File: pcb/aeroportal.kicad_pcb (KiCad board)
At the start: 2 copper layers, 80 x 70 mm, 4 parts, among them J1 MAX98357A Breakout Board, U1 WEMOS_C3_Mini, U2 TFT_ST7735_SD

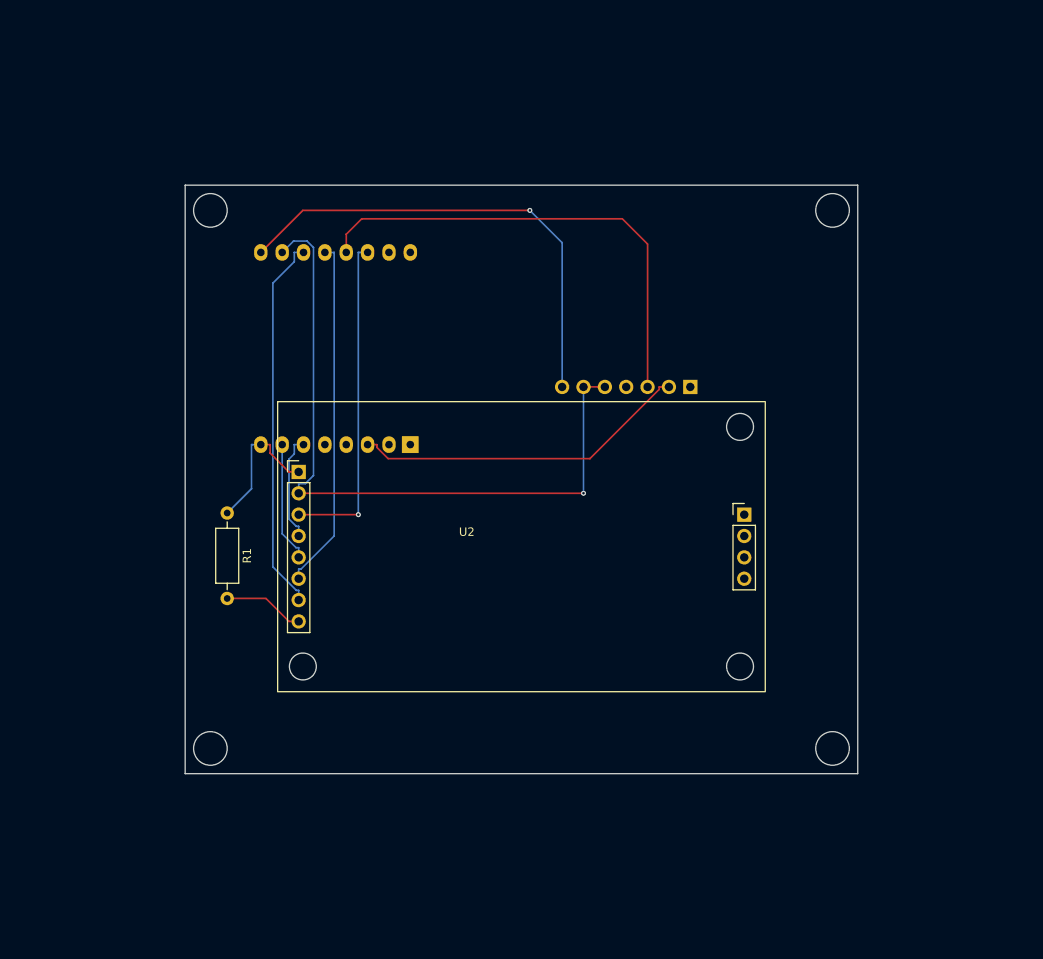
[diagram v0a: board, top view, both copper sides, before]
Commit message: Created case (missing usb hole) and enlarged PCB with hole for speaker
Signed-off-by: Urjith Mishra <66270347+TheScientist101@users.noreply.github.com>
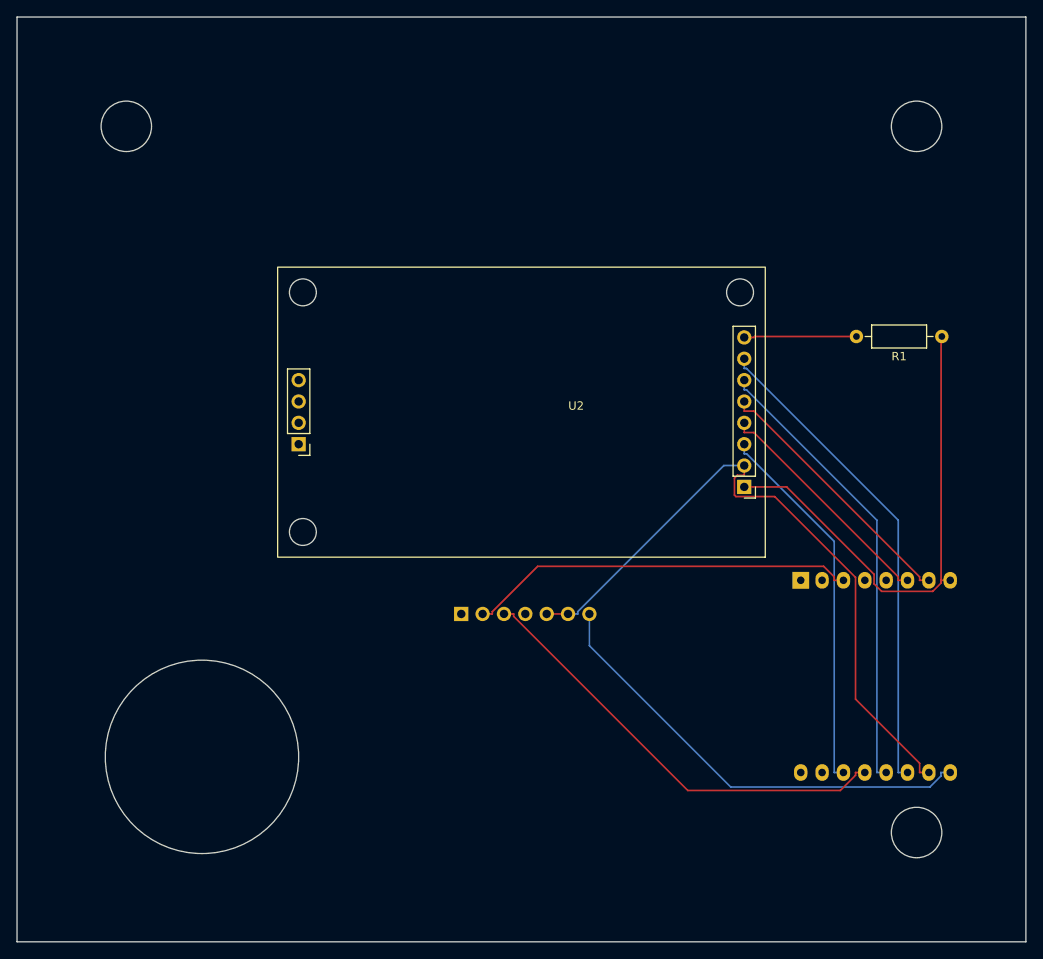
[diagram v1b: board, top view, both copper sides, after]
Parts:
- moved R1 87.6 mm to (197.0, 91.0), turned to 180 degrees
- moved U1 49.2 mm to (180.2, 120.0), turned to -90 degrees
- moved J1 38.4 mm to (139.8, 124.0), turned to -90 degrees
- moved U2 20.2 mm to (153.5, 100.2), turned to 180 degrees
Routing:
- net +3V3: track 16.9 -> 60.1 mm
- net A0: track 14.4 -> 31.7 mm
- net RESET: track 12.9 -> 28.1 mm
- net SCK: track 44.9 -> 58.1 mm
- net MOSI: track 41.8 -> 54.5 mm
- net BCLK: track 40.4 -> 46.4 mm
- net CS: track 39.4 -> 44.8 mm, vias 1 -> 0
- net DIN: track 57.0 -> 52.9 mm
- net Net-(U2-LED): track 9.63 -> 13.4 mm
- net GND: track 84.1 -> 81.4 mm, vias 1 -> 0
- net +5V: track 56.7 -> 54.6 mm, vias 1 -> 0
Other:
- board size 80 x 70 mm -> 120 x 110 mm

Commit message: Remove 0 depth planes in CAD and reroute PCB w/ new LCD model
Signed-off-by: Urjith Mishra <66270347+TheScientist101@users.noreply.github.com>
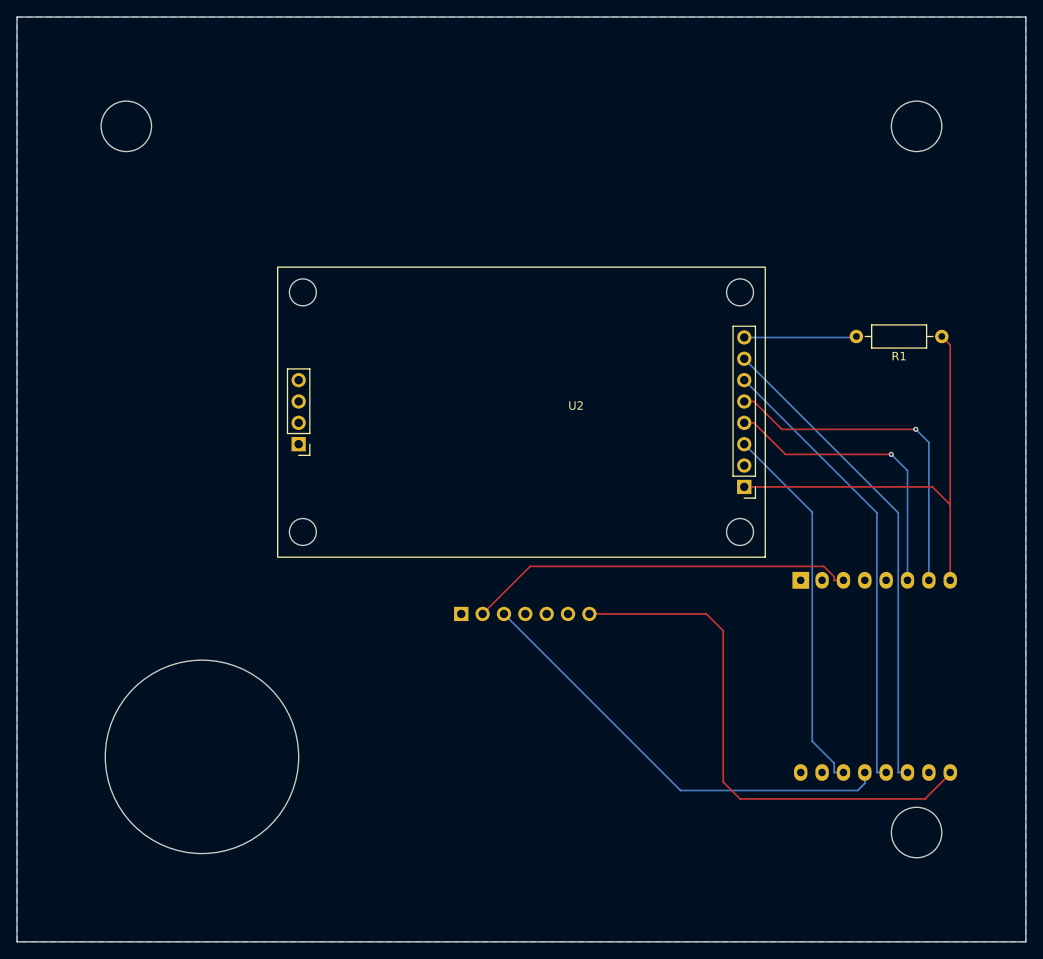
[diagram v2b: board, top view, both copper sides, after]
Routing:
- net GND: track 81.4 -> 0.00 mm
- net +5V: track 54.6 -> 64.0 mm
- net A0: track 31.7 -> 40.4 mm, vias 0 -> 1
- net RESET: track 28.1 -> 34.8 mm, vias 0 -> 1
- net +3V3: track 60.1 -> 54.8 mm
- added copper zone on B.Cu, net GND

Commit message: Created basic firmware and fixed unconnected pin for speaker
Signed-off-by: Urjith Mishra <66270347+TheScientist101@users.noreply.github.com>
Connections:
- U1 pad 2: unconnected-(U1-IO3-Pad2) -> LRC
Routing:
- net LRC: track 0.00 -> 104.6 mm, vias 0 -> 1
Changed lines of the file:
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@@
 	(net 10 "unconnected-(U1-~{RST}-Pad1)")
 	(net 11 "unconnected-(U1-IO1-Pad4)")
-	(net 12 "unconnected-(U1-IO3-Pad2)")
-	(net 13 "unconnected-(U1-IO0-Pad5)")
-	(net 14 "unconnected-(U1-RX-Pad15)")
-	(net 15 "CS")
-	(net 16 "unconnected-(U1-TX-Pad16)")
-	(net 17 "unconnected-(U2-SD_SCK-Pad12)")
-	(net 18 "SCK")
-	(net 19 "unconnected-(U2-SD_CS-Pad9)")
-	(net 20 "unconnected-(U2-SD_MOSI-Pad10)")
-	(net 21 "unconnected-(U2-SD_MISO-Pad11)")
-	(net 22 "Net-(U2-LED)")
-	(net 23 "MOSI")
+	(net 12 "unconnected-(U1-IO0-Pad5)")
+	(net 13 "unconnected-(U1-RX-Pad15)")
+	(net 14 "CS")
+	(net 15 "unconnected-(U1-TX-Pad16)")
+	(net 16 "unconnected-(U2-SD_SCK-Pad12)")
+	(net 17 "SCK")
+	(net 18 "unconnected-(U2-SD_CS-Pad9)")
+	(net 19 "unconnected-(U2-SD_MOSI-Pad10)")
+	(net 20 "unconnected-(U2-SD_MISO-Pad11)")
+	(net 21 "Net-(U2-LED)")
+	(net 22 "MOSI")
 	(footprint "asylum-weather:TFT_ST7735_SD"
 		(layer "F.Cu")
@@
 			(layers "*.Cu" "*.Mask")
 			(remove_unused_layers no)
-			(net 15 "CS")
+			(net 14 "CS")
 			(pinfunction "LCD_CS")
 			(pintype "input")
@@
 			(layers "*.Cu" "*.Mask")
 			(remove_unused_layers no)
-			(net 23 "MOSI")
+			(net 22 "MOSI")
 			(pinfunction "LCD_MOSI")
 			(pintype "input")
@@
 			(layers "*.Cu" "*.Mask")
 			(remove_unused_layers no)
-			(net 18 "SCK")
+			(net 17 "SCK")
 			(pinfunction "LCD_SCK")
 			(pintype "input")
@@
 			(layers "*.Cu" "*.Mask")
 			(remove_unused_layers no)
-			(net 22 "Net-(U2-LED)")
+			(net 21 "Net-(U2-LED)")
 			(pinfunction "LED")
 			(pintype "power_in")
@@
 			(layers "*.Cu" "*.Mask")
 			(remove_unused_layers no)
-			(net 19 "unconnected-(U2-SD_CS-Pad9)")
+			(net 18 "unconnected-(U2-SD_CS-Pad9)")
 			(pinfunction "SD_CS")
 			(pintype "input")
@@
 			(layers "*.Cu" "*.Mask")
 			(remove_unused_layers no)
-			(net 20 "unconnected-(U2-SD_MOSI-Pad10)")
+			(net 19 "unconnected-(U2-SD_MOSI-Pad10)")
 			(pinfunction "SD_MOSI")
 			(pintype "input")
@@
 			(layers "*.Cu" "*.Mask")
 			(remove_unused_layers no)
-			(net 21 "unconnected-(U2-SD_MISO-Pad11)")
+			(net 20 "unconnected-(U2-SD_MISO-Pad11)")
 			(pinfunction "SD_MISO")
 			(pintype "output")
@@
 			(layers "*.Cu" "*.Mask")
 			(remove_unused_layers no)
-			(net 17 "unconnected-(U2-SD_SCK-Pad12)")
+			(net 16 "unconnected-(U2-SD_SCK-Pad12)")
 			(pinfunction "SD_SCK")
 			(pintype "input")
@@
 			(layers "F&B.Cu" "*.Mask")
 			(remove_unused_layers no)
-			(net 22 "Net-(U2-LED)")
+			(net 21 "Net-(U2-LED)")
 			(pintype "passive")
 		)
@@
 			(layers "F&B.Cu" "*.Mask")
 			(remove_unused_layers no)
-			(net 12 "unconnected-(U1-IO3-Pad2)")
+			(net 8 "LRC")
 			(pinfunction "IO3")
 			(pintype "input")
@@
 			(layers "F&B.Cu" "*.Mask")
 			(remove_unused_layers no)
-			(net 13 "unconnected-(U1-IO0-Pad5)")
+			(net 12 "unconnected-(U1-IO0-Pad5)")
 			(pinfunction "IO0")
 			(pintype "bidirectional")
@@
 			(layers "F&B.Cu" "*.Mask")
 			(remove_unused_layers no)
-			(net 18 "SCK")
+			(net 17 "SCK")
 			(pinfunction "SCK/IO6")
 			(pintype "bidirectional")
@@
 			(layers "F&B.Cu" "*.Mask")
 			(remove_unused_layers no)
-			(net 23 "MOSI")
+			(net 22 "MOSI")
 			(pinfunction "MOSI/IO7")
 			(pintype "bidirectional")
@@
 			(layers "F&B.Cu" "*.Mask")
 			(remove_unused_layers no)
-			(net 15 "CS")
+			(net 14 "CS")
 			(pinfunction "CS0/IO10")
 			(pintype "bidirectional")
@@
 			(layers "F&B.Cu" "*.Mask")
 			(remove_unused_layers no)
-			(net 14 "unconnected-(U1-RX-Pad15)")
+			(net 13 "unconnected-(U1-RX-Pad15)")
 			(pinfunction "RX")
 			(pintype "input")
@@
 			(layers "F&B.Cu" "*.Mask")
 			(remove_unused_layers no)
-			(net 16 "unconnected-(U1-TX-Pad16)")
+			(net 15 "unconnected-(U1-TX-Pad16)")
 			(pinfunction "TX")
 			(pintype "output")
@@
 	)
 	(segment
+		(start 202 144)
+		(end 202 141)
+		(width 0.2)
+		(layer "F.Cu")
+		(net 8)
+	)
+	(segment
+		(start 202 141)
+		(end 182.76 121.76)
+		(width 0.2)
+		(layer "F.Cu")
+		(net 8)
+	)
+	(segment
+		(start 182.76 121.76)
+		(end 182.76 120)
+		(width 0.2)
+		(layer "F.Cu")
+		(net 8)
+	)
+	(via
+		(at 202 144)
+		(size 0.6)
+		(drill 0.3)
+		(layers "F.Cu" "B.Cu")
+		(net 8)
+	)
+	(segment
+		(start 161 146)
+		(end 200 146)
+		(width 0.2)
+		(layer "B.Cu")
+		(net 8)
+	)
+	(segment
+		(start 139.84 124.84)
+		(end 161 146)
+		(width 0.2)
+		(layer "B.Cu")
+		(net 8)
+	)
+	(segment
+		(start 139.84 124)
+		(end 139.84 124.84)
+		(width 0.2)
+		(layer "B.Cu")
+		(net 8)
+	)
+	(segment
+		(start 200 146)
+		(end 202 144)
+		(width 0.2)
+		(layer "B.Cu")
+		(net 8)
+	)
+	(segment
 		(start 178.4029 105.0212)
 		(end 174.6517 101.27)
@@
 		(width 0.2)
 		(layer "B.Cu")
-		(net 15)
+		(net 14)
 	)
 	(segment
@@
 		(width 0.2)
 		(layer "B.Cu")
-		(net 15)
+		(net 14)
 	)
 	(segment
@@
 		(width 0.2)
 		(layer "B.Cu")
-		(net 15)
+		(net 14)
 	)
 	(segment
@@
 		(width 0.2)
 		(layer "B.Cu")
-		(net 15)
+		(net 14)
 	)
 	(segment
@@
 		(width 0.2)
 		(layer "B.Cu")
-		(net 15)
+		(net 14)
 	)
 	(segment
@@
 		(width 0.2)
 		(layer "B.Cu")
-		(net 18)
+		(net 17)
 	)
 	(segment
@@
 		(width 0.2)
 		(layer "B.Cu")
-		(net 18)
+		(net 17)
 	)
 	(segment
@@
 		(width 0.2)
 		(layer "B.Cu")
-		(net 18)
+		(net 17)
 	)
 	(segment
@@
 		(width 0.2)
 		(layer "B.Cu")
-		(net 22)
+		(net 21)
 	)
 	(segment
@@
 		(width 0.2)
 		(layer "B.Cu")
-		(net 22)
+		(net 21)
 	)
 	(segment
@@
 		(width 0.2)
 		(layer "B.Cu")
-		(net 23)
+		(net 22)
 	)
 	(segment
@@
 		(width 0.2)
 		(layer "B.Cu")
-		(net 23)
+		(net 22)
 	)
 	(segment
@@
 		(width 0.2)
 		(layer "B.Cu")
-		(net 23)
+		(net 22)
 	)
 	(zone

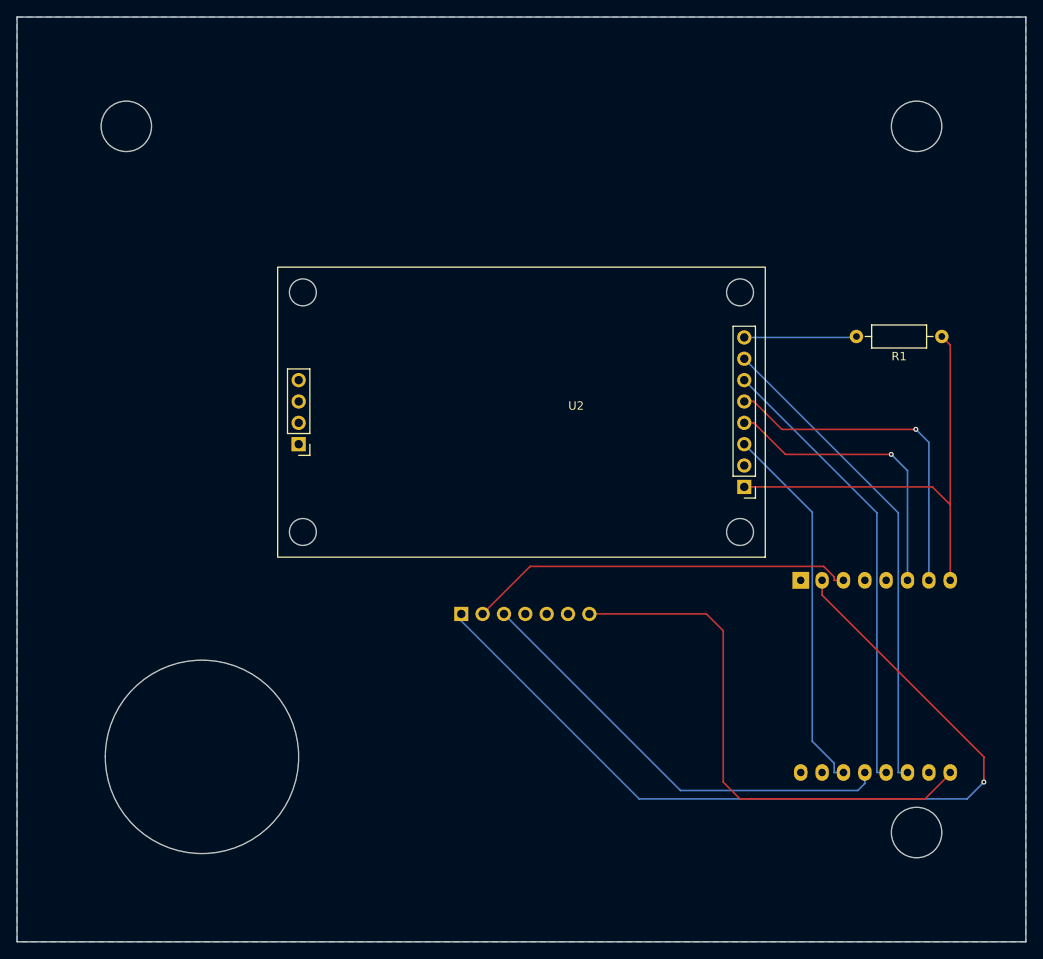
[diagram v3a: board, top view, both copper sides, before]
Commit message: Reduced pcb size to 100mm x 100mm to reduce costs
Signed-off-by: Urjith Mishra <66270347+TheScientist101@users.noreply.github.com>
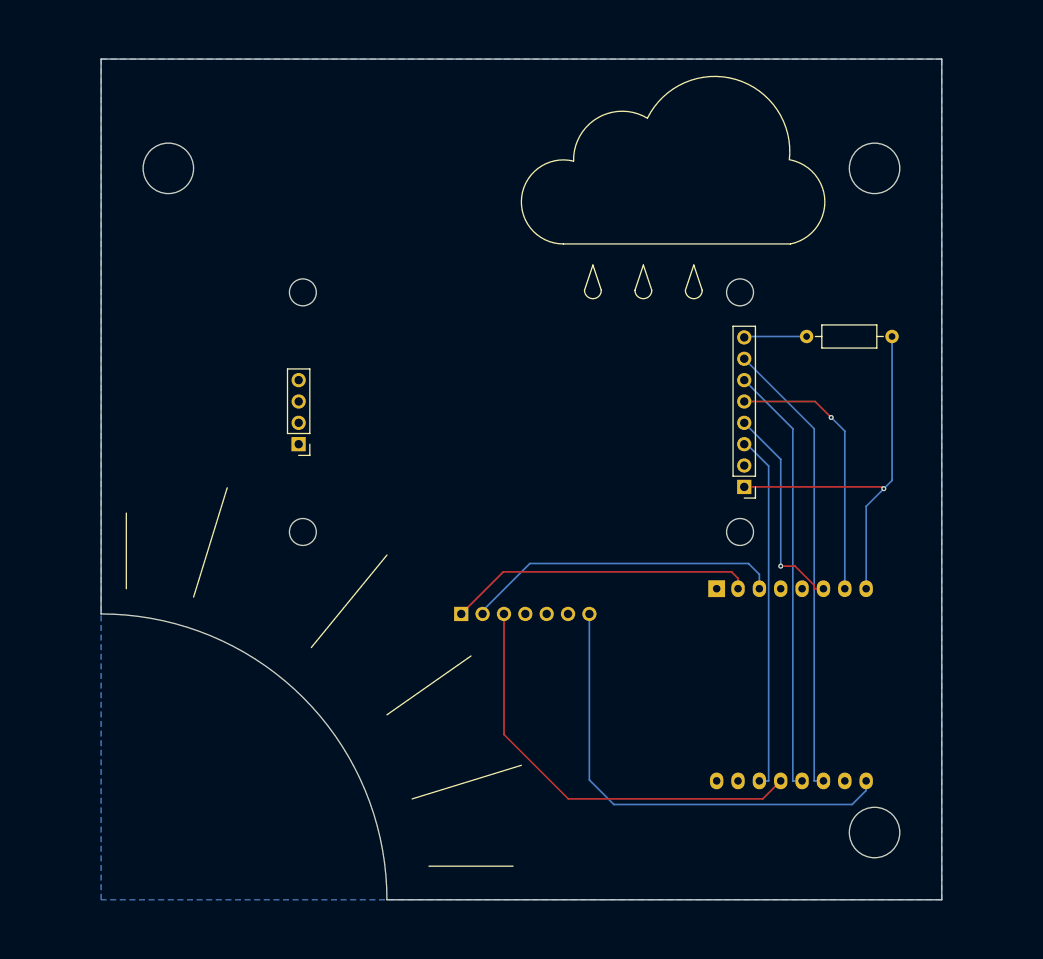
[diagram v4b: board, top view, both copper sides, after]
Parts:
- moved U1 10.0 mm to (170.2, 121.0)
- moved R1 5.92 mm to (191.1, 91.0)
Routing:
- net LRC: track 104.6 -> 36.5 mm, vias 1 -> 0
- net RESET: track 34.8 -> 25.3 mm
- net BCLK: track 46.2 -> 37.9 mm
- net +5V: track 64.0 -> 55.7 mm
- net A0: track 40.4 -> 32.2 mm
- net +3V3: track 54.8 -> 48.0 mm, vias 0 -> 1
- net Net-(U2-LED): track 13.4 -> 7.47 mm
- net SCK: track 57.9 -> 54.8 mm
- net MOSI: track 54.3 -> 51.2 mm
- net CS: track 44.6 -> 42.5 mm
- net DIN: track 53.3 -> 51.3 mm
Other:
- board size 120 x 110 mm -> 100 x 100 mm
